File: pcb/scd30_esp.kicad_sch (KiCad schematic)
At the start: 36 parts, among them J1 SCD30, J2 USB_C_Receptacle_USB2.0, J4 QWIIC, Q2 Q_NMOS_GSD, Q3 BSS138PS, Q4 Q_NMOS_GSD, SW1 SW_SPST, U1 TPS62A01PDDCR, U2 ESP32-WROOM-E, U3 CH340C, U4 TSOP38G36

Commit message: RC1
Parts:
- added D7: LED_Small, LED_SMD:LED_0603_1608Metric, symbol Device:LED_Small
- added R17: 1k, Resistor_SMD:R_0603_1608Metric, symbol Device:R_Small
- D5, D6: LCSC (none) -> C511094
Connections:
- net GND: now also D7.1 (K)
- net status_led: now reaches U2.24 (ADC2_CH2/GPIO2)
- net status_led: now also R17.2
- new net: D7.2 (A), R17.1
- no-connect marks 16 -> 15
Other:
- moved on the sheet: U2

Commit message: Added JLCPCB production files
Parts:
- SW1: LCSC (none) -> C512395
- U2: LCSC (none) -> C701342
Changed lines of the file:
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@@
+			)
+		)
+		(property "LCSC" "C701342"
+			(at 73.3141 105.41 0)
+			(effects
+				(font
+					(size 1.27 1.27)
+				)
+				(hide yes)
 			)
 		)
@@
 			(effects
 				(font
+					(size 1.27 1.27)
+				)
+				(hide yes)
+			)
+		)
+		(property "LCSC" "C512395"
+			(at 147.32 146.304 0)
+			(effects
+				(font

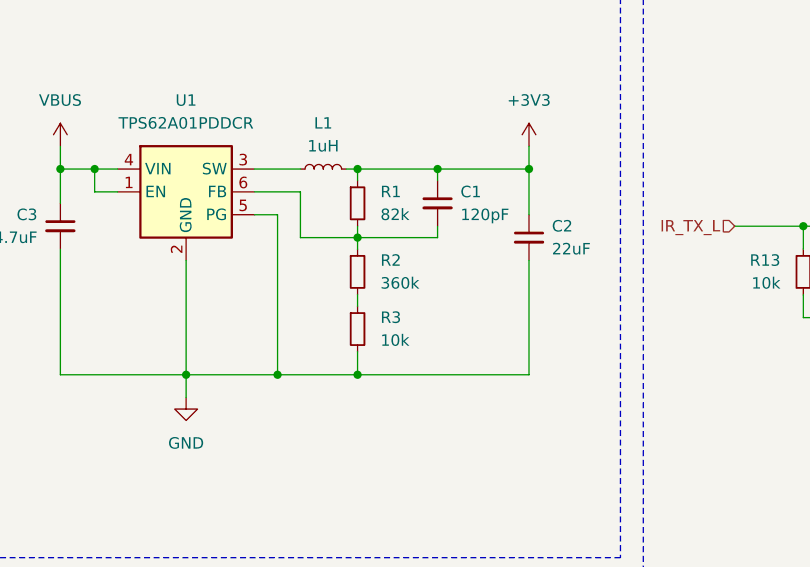
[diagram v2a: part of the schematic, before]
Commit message: Added factory reset
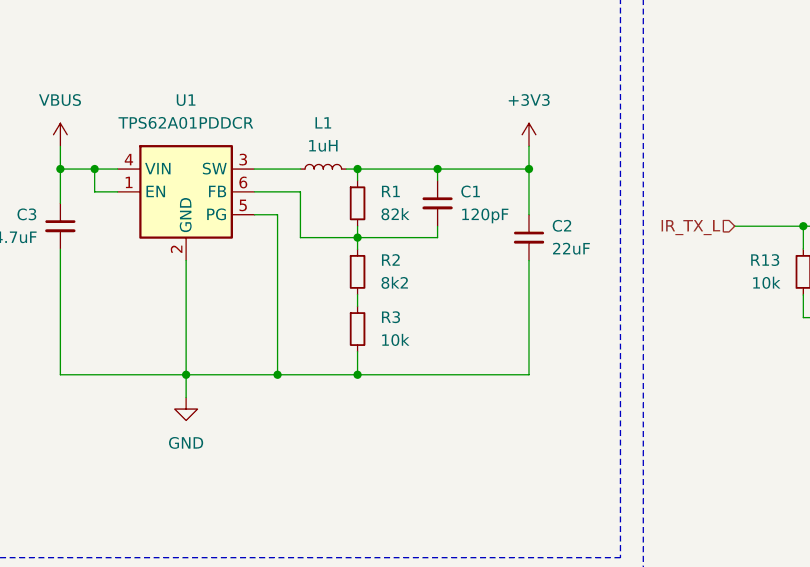
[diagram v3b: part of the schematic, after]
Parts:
- R2: value 360k -> 8k2
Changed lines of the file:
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@@
 			)
 		)
-		(property "Value" "360k"
+		(property "Value" "8k2"
 			(at 184.15 58.4199 0)
 			(effects
